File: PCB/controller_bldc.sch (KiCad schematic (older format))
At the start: 72 parts, among them J1 Battery Supply, J2 Conn_01x11_Male, J6 LM35, J7 Hall Sensors, J9 BLDC Motor, K1 RAYEX-L90B, Q1 IRF1010N, Q2 IRF1010N, Q3 IRF1010N, Q4 IRF1010N, Q5 IRF1010N, Q6 IRF1010N, Q7 PN2222A, SW1 ON_OFF, U1 ESP32-DEVKITC-32D, U2 MC1458P, U3 LM2596SOURCE_Pin2, U4 IR2103, U5 LM2596SOURCE, U8 IR2103, U9 IR2103

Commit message: PCB v1.1 with the res. for throttle
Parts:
- added R29: 2.5k, Resistor_THT:R_Axial_DIN0207_L6.3mm_D2.5mm_P10.16mm_Horizontal, symbol Device:R
- U2: symbol MC1458P:MC1458P -> controller_bldc-rescue:MC1458P-MC1458P
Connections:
- net labels added: Throttle_Raw
- wire segments 280 -> 282
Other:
- moved on the sheet: R12, R26, R27
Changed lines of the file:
@@
 	1    0    0    -1
 $EndComp
-Text GLabel 6150 750  2    50   Input ~ 0
+Text GLabel 5750 3350 0    50   Input ~ 0
 Throttle
 $Comp
@@
 Text GLabel 7450 2600 0    50   Input ~ 0
 HIN1
-Text GLabel 6900 950  2    50   Input ~ 0
+Text GLabel 7050 950  2    50   Input ~ 0
 Brake
 Text GLabel 6500 5050 2    50   Input ~ 0
@@
 L Device:R R12
 U 1 1 6097CC14
-P 6800 650
-F 0 "R12" H 6870 696 50  0000 L CNN
-F 1 "1.5k" V 6800 550 50  0000 L CNN
-F 2 "Resistor_THT:R_Axial_DIN0207_L6.3mm_D2.5mm_P10.16mm_Horizontal" V 6730 650 50  0001 C CNN
-F 3 "~" H 6800 650 50  0001 C CNN
-	1    6800 650
+P 6950 650
+F 0 "R12" H 7020 696 50  0000 L CNN
+F 1 "1.5k" V 6950 550 50  0000 L CNN
+F 2 "Resistor_THT:R_Axial_DIN0207_L6.3mm_D2.5mm_P10.16mm_Horizontal" V 6880 650 50  0001 C CNN
+F 3 "~" H 6950 650 50  0001 C CNN
+	1    6950 650
 	1    0    0    -1
 $EndComp
@@
 L power:+3V3 #PWR0111
 U 1 1 6099D286
-P 6800 450
-F 0 "#PWR0111" H 6800 300 50  0001 C CNN
-F 1 "+3V3" H 6815 623 50  0000 C CNN
-F 2 "" H 6800 450 50  0001 C CNN
-F 3 "" H 6800 450 50  0001 C CNN
-	1    6800 450
-	1    0    0    -1
-$EndComp
-Wire Wire Line
-	6800 800  6800 950
-Wire Wire Line
-	6800 950  6900 950
-Connection ~ 6800 950
+P 6950 450
+F 0 "#PWR0111" H 6950 300 50  0001 C CNN
+F 1 "+3V3" H 6965 623 50  0000 C CNN
+F 2 "" H 6950 450 50  0001 C CNN
+F 3 "" H 6950 450 50  0001 C CNN
+	1    6950 450
+	1    0    0    -1
+$EndComp
+Wire Wire Line
+	6950 800  6950 950
+Wire Wire Line
+	6950 950  7050 950
+Connection ~ 6950 950
 $Comp
 L power:GND #PWR0112
@@
 $EndComp
 Wire Wire Line
-	6800 450  6800 500
+	6950 450  6950 500
 $Comp
 L Device:R R11
@@
 L power:+5V #PWR0113
 U 1 1 60B56613
-P 6600 850
-F 0 "#PWR0113" H 6600 700 50  0001 C CNN
-F 1 "+5V" H 6615 1023 50  0000 C CNN
-F 2 "" H 6600 850 50  0001 C CNN
-F 3 "" H 6600 850 50  0001 C CNN
-	1    6600 850
+P 6750 850
+F 0 "#PWR0113" H 6750 700 50  0001 C CNN
+F 1 "+5V" H 6765 1023 50  0000 C CNN
+F 2 "" H 6750 850 50  0001 C CNN
+F 3 "" H 6750 850 50  0001 C CNN
+	1    6750 850
 	1    0    0    -1
 $EndComp
@@
 	2650 7900 2650 7950
 $Comp
-L MC1458P:MC1458P U2
+L controller_bldc-rescue:MC1458P-MC1458P U2
 U 1 1 608585E5
 P 4650 2600
@@
 Wire Wire Line
 	5800 2150 5800 2200
-Text GLabel 5400 3600 0    50   Input ~ 0
+Text GLabel 5750 3700 0    50   Input ~ 0
 Current_Sensor_IN
-Text GLabel 6100 3600 2    50   Input ~ 0
+Text GLabel 6450 3700 2    50   Input ~ 0
 1IN-
 $Comp
 L Device:R R26
 U 1 1 613AAA2C
-P 5750 3600
-F 0 "R26" V 5650 3600 50  0000 C CNN
-F 1 "2.5k" V 5750 3600 50  0000 C CNN
-F 2 "Resistor_THT:R_Axial_DIN0207_L6.3mm_D2.5mm_P10.16mm_Horizontal" V 5680 3600 50  0001 C CNN
-F 3 "~" H 5750 3600 50  0001 C CNN
-	1    5750 3600
-	0    1    1    0
-$EndComp
-Wire Wire Line
-	5400 3600 5600 3600
-Wire Wire Line
-	5900 3600 6100 3600
-Text GLabel 5400 3950 0    50   Input ~ 0
+P 6100 3700
+F 0 "R26" V 6000 3700 50  0000 C CNN
+F 1 "2.5k" V 6100 3700 50  0000 C CNN
+F 2 "Resistor_THT:R_Axial_DIN0207_L6.3mm_D2.5mm_P10.16mm_Horizontal" V 6030 3700 50  0001 C CNN
+F 3 "~" H 6100 3700 50  0001 C CNN
+	1    6100 3700
+	0    1    1    0
+$EndComp
+Wire Wire Line
+	5750 3700 5950 3700
+Wire Wire Line
+	6250 3700 6450 3700
+Text GLabel 5750 4050 0    50   Input ~ 0
 LM35
-Text GLabel 6100 3950 2    50   Input ~ 0
+Text GLabel 6450 4050 2    50   Input ~ 0
 2IN-
 $Comp
 L Device:R R27
 U 1 1 6140BDEB
-P 5750 3950
-F 0 "R27" V 5650 3950 50  0000 C CNN
-F 1 "2.5k" V 5750 3950 50  0000 C CNN
-F 2 "Resistor_THT:R_Axial_DIN0207_L6.3mm_D2.5mm_P10.16mm_Horizontal" V 5680 3950 50  0001 C CNN
-F 3 "~" H 5750 3950 50  0001 C CNN
-	1    5750 3950
-	0    1    1    0
-$EndComp
-Wire Wire Line
-	5400 3950 5600 3950
-Wire Wire Line
-	5900 3950 6100 3950
+P 6100 4050
+F 0 "R27" V 6000 4050 50  0000 C CNN
+F 1 "2.5k" V 6100 4050 50  0000 C CNN
+F 2 "Resistor_THT:R_Axial_DIN0207_L6.3mm_D2.5mm_P10.16mm_Horizontal" V 6030 4050 50  0001 C CNN
+F 3 "~" H 6100 4050 50  0001 C CNN
+	1    6100 4050
+	0    1    1    0
+$EndComp
+Wire Wire Line
+	5750 4050 5950 4050
+Wire Wire Line
+	6250 4050 6450 4050
 Wire Wire Line
 	4550 5050 4750 5050
@@
 	6050 1050 6200 1050
 Wire Wire Line
-	6050 950  6800 950
-Wire Wire Line
-	6050 850  6600 850
-Wire Wire Line
 	6050 750  6150 750
 Wire Wire Line
@@
 $EndComp
 $Comp
-L power:-5V #PWR?
+L power:-5V #PWR0137
 U 1 1 608A9160
 P 3350 5600
-F 0 "#PWR?" H 3350 5700 50  0001 C CNN
+F 0 "#PWR0137" H 3350 5700 50  0001 C CNN
 F 1 "-5V" H 3365 5773 50  0000 C CNN
 F 2 "" H 3350 5600 50  0001 C CNN
@@
 	3350 5700 3350 5600
 Connection ~ 3350 5700
+Text GLabel 6150 750  2    50   Input ~ 0
+Throttle_Raw
+Wire Wire Line
+	6050 850  6750 850
+Wire Wire Line
+	6050 950  6950 950
+Text GLabel 6450 3350 2    50   Input ~ 0
+Throttle_Raw
+$Comp
+L Device:R R29
+U 1 1 6094A225
+P 6100 3350
+F 0 "R29" V 6000 3350 50  0000 C CNN
+F 1 "2.5k" V 6100 3350 50  0000 C CNN
+F 2 "Resistor_THT:R_Axial_DIN0207_L6.3mm_D2.5mm_P10.16mm_Horizontal" V 6030 3350 50  0001 C CNN
+F 3 "~" H 6100 3350 50  0001 C CNN
+	1    6100 3350
+	0    1    1    0
+$EndComp
+Wire Wire Line
+	6250 3350 6450 3350
+Wire Wire Line
+	5750 3350 5950 3350
 $EndSCHEMATC

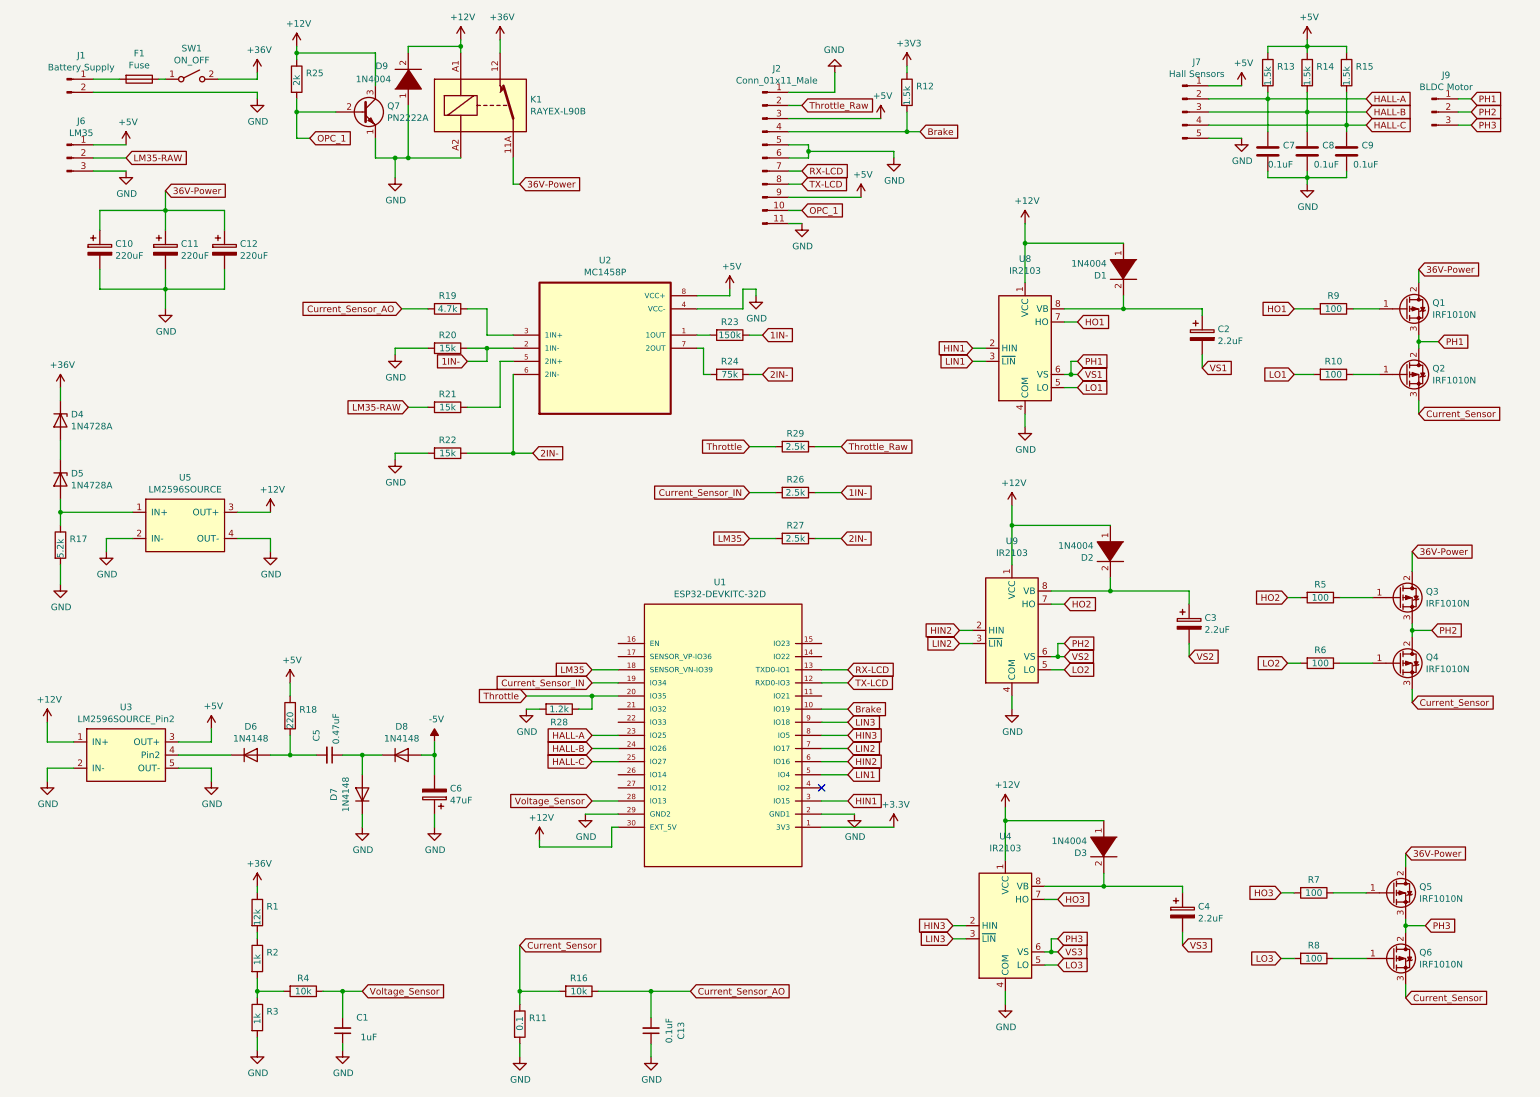
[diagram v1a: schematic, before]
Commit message: README updated with DC-DC converter's datasheet Closes #11
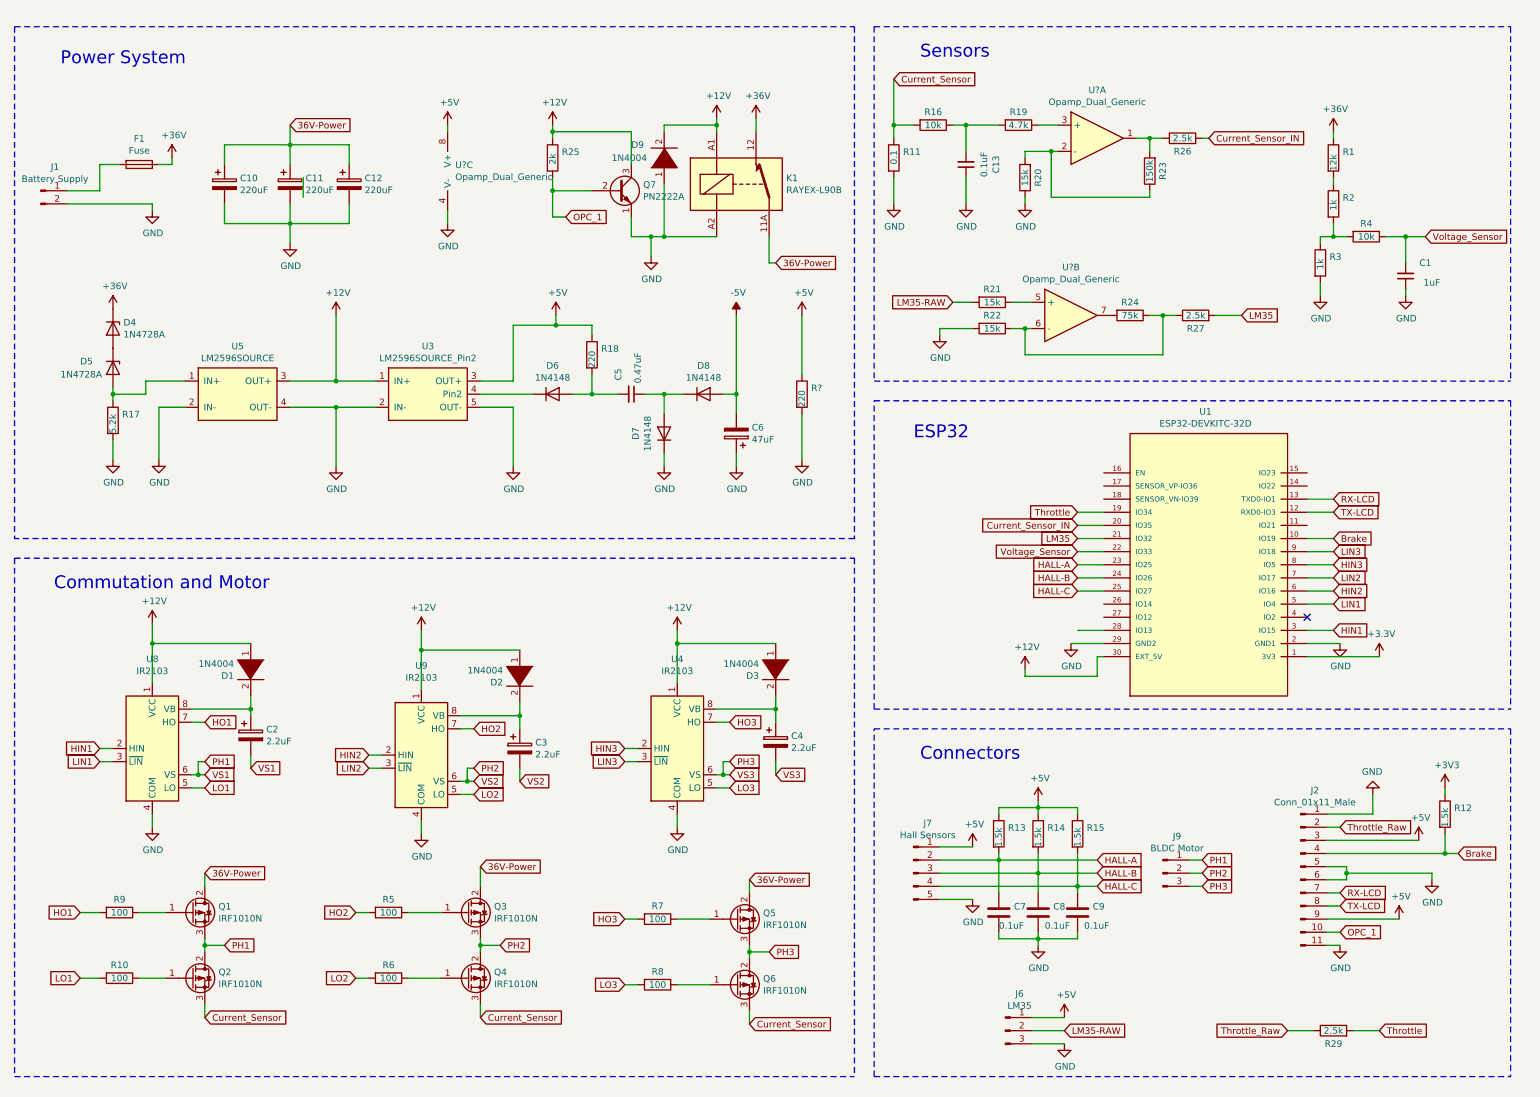
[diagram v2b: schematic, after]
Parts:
- removed R28: 1.2k, Resistor_THT:R_Axial_DIN0207_L6.3mm_D2.5mm_P10.16mm_Horizontal, symbol Device:R
- removed SW1: ON_OFF, Connector_Molex:Molex_KK-254_AE-6410-02A_1x02_P2.54mm_Vertical, symbol Switch:SW_SPST
- removed U2: MC1458P, Package_DIP:DIP-8_W7.62mm_LongPads, symbol controller_bldc-rescue:MC1458P-MC1458P
- added R?: 220, Resistor_THT:R_Axial_DIN0207_L6.3mm_D2.5mm_P10.16mm_Horizontal, symbol Device:R
- added U? (x3): Opamp_Dual_Generic, Package_DIP:DIP-8_W7.62mm_LongPads, symbol Device:Opamp_Dual_Generic
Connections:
- net +36V: now also F1.1
- net +5V: now also R?.1, U?.8 (V+)
- net Current_Sensor_IN: now also U1.20 (IO35); no longer U1.19 (IO34)
- net GND: now also R20.1, R?.2, U?.4 (V-); no longer R20.2
- net LM35: now also U1.21 (IO32); no longer U1.18 (SENSOR_VN-IO39)
- net Throttle: now also U1.19 (IO34); no longer U1.20 (IO35)
- net Voltage_Sensor: now also U1.22 (IO33); no longer U1.28 (IO13)
- net at R23.2: now also R26.1, U?.1
- net at R19.1: now also U?.3 (+)
- net at R21.1: now also U?.5 (+)
- net at R24.2: now also U?.7
- removed net 1IN-: R20.1, R23.1, R26.1
- net 2IN-: no longer names the net of R22.1, R24.1, R27.1
- net 2IN-: now also U?.6 (-)
- net Current_Sensor_AO: no longer names the net of C13.2, R16.1, R19.2
- new net: R20.2, R23.1, U?.2 (-)
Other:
- note added: "Commutation and Motor\n"
- note added: "Connectors\n"
- note added: "ESP32\n"
- note added: "Power System\n"
- note added: "Sensors"
- moved on the sheet: C1, C10, C11, C12, C13, C2, C3, C4, C5, C6, C7, C8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

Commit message: PCB working, printing sensors in a good-looking console Fixed the issue with multiple sensors affected when overvoltage in throttle. Closes #16, closes #17, closes #18
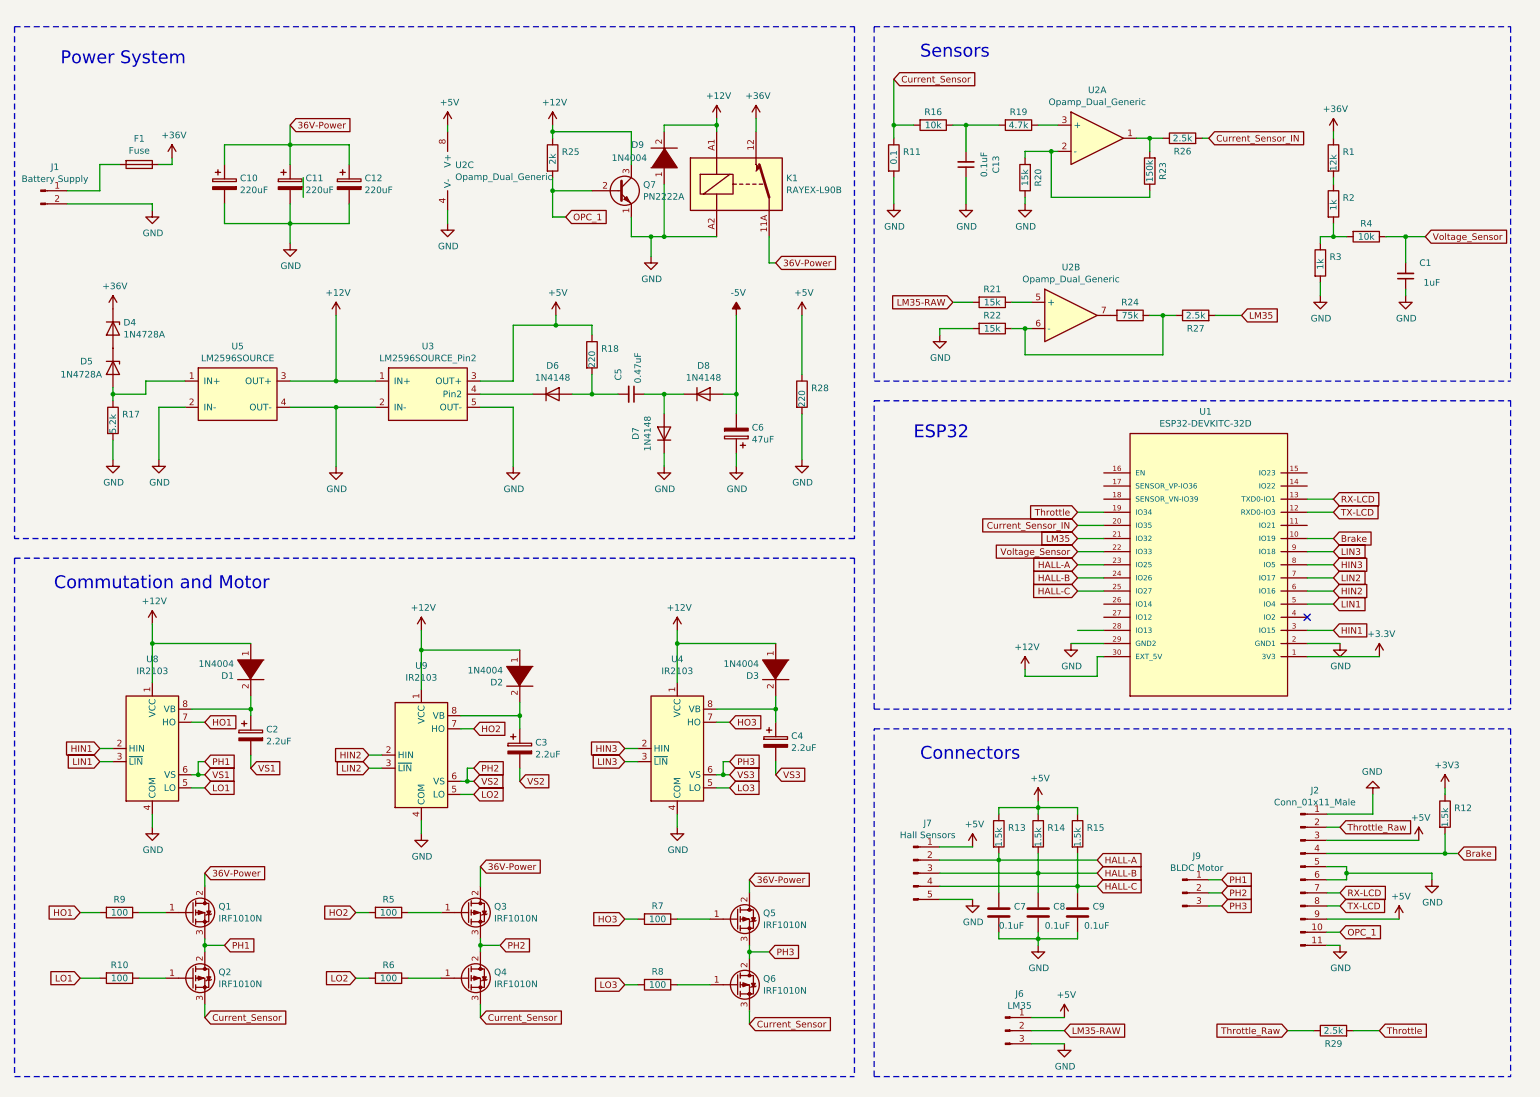
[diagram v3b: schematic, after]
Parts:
- gave numbers to parts that had none: 2
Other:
- moved on the sheet: J9
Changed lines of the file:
@@
 	2900 2850 2600 2850
 $Comp
-L power:+12V #PWR?
+L power:+12V #PWR0120
 U 1 1 61AD3724
 P 2600 2350
-F 0 "#PWR?" H 2600 2200 50  0001 C CNN
+F 0 "#PWR0120" H 2600 2200 50  0001 C CNN
 F 1 "+12V" H 2615 2523 50  0000 C CNN
 F 2 "" H 2600 2350 50  0001 C CNN
@@
 	4275 2425 4275 2350
 $Comp
-L power:+5V #PWR?
+L power:+5V #PWR0121
 U 1 1 618BBD75
 P 4275 2350
-F 0 "#PWR?" H 4275 2200 50  0001 C CNN
+F 0 "#PWR0121" H 4275 2200 50  0001 C CNN
 F 1 "+5V" H 4290 2523 50  0000 C CNN
 F 2 "" H 4275 2350 50  0001 C CNN
@@
 36V-Power
 $Comp
-L Device:Opamp_Dual_Generic U?
+L Device:Opamp_Dual_Generic U2
 U 3 1 60CF4CB9
 P 3550 1250
-F 0 "U?" H 3508 1296 50  0000 L CNN
+F 0 "U2" H 3508 1296 50  0000 L CNN
 F 1 "Opamp_Dual_Generic" H 3508 1205 50  0000 L CNN
 F 2 "Package_DIP:DIP-8_W7.62mm_LongPads" H 3550 1250 50  0001 C CNN
@@
 	7850 2650 8900 2650
 $Comp
-L Device:Opamp_Dual_Generic U?
+L Device:Opamp_Dual_Generic U2
 U 2 1 60CF35EA
 P 8200 2350
-F 0 "U?" H 8200 2717 50  0000 C CNN
+F 0 "U2" H 8200 2717 50  0000 C CNN
 F 1 "Opamp_Dual_Generic" H 8200 2626 50  0000 C CNN
 F 2 "Package_DIP:DIP-8_W7.62mm_LongPads" H 8200 2350 50  0001 C CNN
@@
 $EndComp
 $Comp
-L Device:Opamp_Dual_Generic U?
+L Device:Opamp_Dual_Generic U2
 U 1 1 60CF1C51
 P 8400 1000
-F 0 "U?" H 8400 1367 50  0000 C CNN
+F 0 "U2" H 8400 1367 50  0000 C CNN
 F 1 "Opamp_Dual_Generic" H 8400 1276 50  0000 C CNN
 F 2 "Package_DIP:DIP-8_W7.62mm_LongPads" H 8400 1000 50  0001 C CNN
@@
 L Connector:Conn_01x03_Male J9
 U 1 1 6069B167
-P 8900 6600
-F 0 "J9" H 9008 6881 50  0000 C CNN
-F 1 "BLDC Motor" H 9008 6790 50  0000 C CNN
-F 2 "Connector_Phoenix_GMSTB:PhoenixContact_GMSTBA_2,5_3-G-7,62_1x03_P7.62mm_Horizontal" H 8900 6600 50  0001 C CNN
-F 3 "~" H 8900 6600 50  0001 C CNN
-	1    8900 6600
-	1    0    0    -1
-$EndComp
-Text GLabel 9200 6500 2    50   Input ~ 0
+P 9050 6750
+F 0 "J9" H 9158 7031 50  0000 C CNN
+F 1 "BLDC Motor" H 9158 6940 50  0000 C CNN
+F 2 "Connector_Phoenix_GMSTB:PhoenixContact_GMSTBA_2,5_3-G-7,62_1x03_P7.62mm_Horizontal" H 9050 6750 50  0001 C CNN
+F 3 "~" H 9050 6750 50  0001 C CNN
+	1    9050 6750
+	1    0    0    -1
+$EndComp
+Text GLabel 9350 6650 2    50   Input ~ 0
 PH1
-Text GLabel 9200 6600 2    50   Input ~ 0
+Text GLabel 9350 6750 2    50   Input ~ 0
 PH2
-Text GLabel 9200 6700 2    50   Input ~ 0
+Text GLabel 9350 6850 2    50   Input ~ 0
 PH3
 Wire Wire Line
-	9100 6500 9200 6500
-Wire Wire Line
-	9100 6600 9200 6600
-Wire Wire Line
-	9100 6700 9200 6700
+	9250 6650 9350 6650
+Wire Wire Line
+	9250 6750 9350 6750
+Wire Wire Line
+	9250 6850 9350 6850
 Wire Wire Line
 	7950 7150 7950 7100
@@
 	6850 900  7000 900
 $Comp
-L power:+5V #PWR?
+L power:+5V #PWR0122
 U 1 1 62B299D0
 P 6150 2350
-F 0 "#PWR?" H 6150 2200 50  0001 C CNN
+F 0 "#PWR0122" H 6150 2200 50  0001 C CNN
 F 1 "+5V" H 6165 2523 50  0000 C CNN
 F 2 "" H 6150 2350 50  0001 C CNN
@@
 $EndComp
 $Comp
-L Device:R R?
+L Device:R R28
 U 1 1 62B2AA51
 P 6150 2950
-F 0 "R?" H 6220 2996 50  0000 L CNN
+F 0 "R28" H 6220 2996 50  0000 L CNN
 F 1 "220" V 6150 2850 50  0000 L CNN
 F 2 "Resistor_THT:R_Axial_DIN0207_L6.3mm_D2.5mm_P10.16mm_Horizontal" V 6080 2950 50  0001 C CNN
@@
 	3950 3050 3950 3500
 $Comp
-L power:GND #PWR?
+L power:GND #PWR0126
 U 1 1 62B97047
 P 6150 3450
-F 0 "#PWR?" H 6150 3200 50  0001 C CNN
+F 0 "#PWR0126" H 6150 3200 50  0001 C CNN
 F 1 "GND" H 6155 3277 50  0000 C CNN
 F 2 "" H 6150 3450 50  0001 C CNN
